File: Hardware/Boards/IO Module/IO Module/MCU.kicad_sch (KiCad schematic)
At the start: 0 parts

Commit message: Updated IO Module Schematics
Added Power, USB hub and USB-JTAG circuits
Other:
- company: (none) -> Drexel University
- title: (none) -> MCU
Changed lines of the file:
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@@
 	(generator "eeschema")
 	(generator_version "8.0")
-	(paper "A4")
+	(paper "A3")
+	(title_block
+		(title "MCU")
+		(date "2024-07-14")
+		(rev "1.0")
+		(company "Drexel University")
+		(comment 1 "Designed by John Hofmeyr")
+	)
 )

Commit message: Updated IO Module Schematics
Added MCU, JTAG and FIFO circuits
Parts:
- added C100, C101: 18pF, Capacitor_SMD:C_0402_1005Metric, symbol Device:C_Small
- added C102, C103, C104, C105, C106, C107, C108, C109, C110, C112: 100nF, Capacitor_SMD:C_0402_1005Metric, symbol Device:C_Small
- added D6: MCU Heartbeat, LED_SMD:LED_0603_1608Metric, symbol Device:LED
- added R66: 10K, Resistor_SMD:R_0402_1005Metric, symbol Device:R_US
- added R67: 1K, Resistor_SMD:R_0402_1005Metric, symbol Device:R_US
- added SW2: RST, Button_Switch_SMD:SW_SPST_PTS645, symbol Switch:SW_SPST
- added TP3, TP4: TestPoint, TestPoint:TestPoint_Pad_D1.0mm, symbol Connector:TestPoint
- added U17: RP2040, Package_DFN_QFN:QFN-56-1EP_7x7mm_P0.4mm_EP3.2x3.2mm, symbol MCU_RaspberryPi:RP2040
- added U19: W25Q16JVUXIQ TR, FursuitTurbofan:USON-8_UX_2x3x0p6_WIN, symbol Memory_Flash:W25Q16JVUXIQ_TR
- added Y5: 12Mhz, Oscillator:Oscillator_SMD_Abracon_ASE-4Pin_3.2x2.5mm, symbol Device:Crystal_GND24_Small
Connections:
- new net: TP3.1, U17.24 (SWCLK)
- new net: TP4.1, U17.25 (SWD)
- new net: R67.1, U17.37 (GPIO25)
- new net: R66.2, SW2.2 (B)
- new net: D6.2 (A), R67.2
- new net +3V3: C105.1, C106.1, C107.1, C108.1, C109.1, C110.1, C112.1, U17.1 (IOVDD), U17.10 (IOVDD), U17.22 (IOVDD), U17.33 (IOVDD), U17.42 (IOVDD), U17.43 (ADC_AVDD), U17.44 (VREG_IN), U17.48 (USB_VDD), U17.49 (IOVDD), U19.8 (VCC)
- new net GND: C100.2, C101.2, C102.2, C103.2, C104.2, C105.2, C106.2, C107.2, C108.2, C109.2, C110.2, C112.2, D6.1 (K), SW2.1 (A), U17.19 (TESTEN), U17.57 (GND), U19.4 (GND), U19.9 (EPAD), Y5.2, Y5.4
- new net I2C0_SCL: U17.7 (GPIO5)
- new net I2C0_SDA: U17.6 (GPIO4)
- new net I2C1_SCL: U17.9 (GPIO7)
- new net I2C1_SDA: U17.8 (GPIO6)
- new net MBUS_D0: U17.11 (GPIO8)
- new net MBUS_D1: U17.12 (GPIO9)
- new net MBUS_D10: U17.29 (GPIO18)
- new net MBUS_D11: U17.30 (GPIO19)
- new net MBUS_D12: U17.31 (GPIO20)
- new net MBUS_D13: U17.32 (GPIO21)
- new net MBUS_D14: U17.34 (GPIO22)
- new net MBUS_D15: U17.35 (GPIO23)
- new net MBUS_D2: U17.13 (GPIO10)
- new net MBUS_D3: U17.14 (GPIO11)
- new net MBUS_D4: U17.15 (GPIO12)
- new net MBUS_D5: U17.16 (GPIO13)
- new net MBUS_D6: U17.17 (GPIO14)
- new net MBUS_D7: U17.18 (GPIO15)
- new net MBUS_D8: U17.27 (GPIO16)
- new net MBUS_D9: U17.28 (GPIO17)
- new net MCU_1V1: C102.1, C103.1, C104.1, U17.23 (DVDD), U17.45 (VREG_VOUT), U17.50 (DVDD)
- new net MCU_XI: C100.1, U17.20 (XIN), Y5.1
- new net MCU_XO: C101.1, U17.21 (XOUT), Y5.3
- new net QSPI_CLK: U17.52 (QSPI_SCLK), U19.6 (CLK)
- new net QSPI_CS: R66.1, U17.56 (QSPI_SS), U19.1 (/CS)
- new net QSPI_D0: U17.53 (QSPI_SD0), U19.5 (DI(IO0))
- new net QSPI_D1: U17.55 (QSPI_SD1), U19.2 (DO(IO1))
- new net QSPI_D2: U17.54 (QSPI_SD2), U19.3 (/WP(IO2))
- new net QSPI_D3: U17.51 (QSPI_SD3), U19.7 (/HLD/RST(IO3))
- new net USB_MCU_D_N: U17.46 (USB_DM)
- new net USB_MCU_D_P: U17.47 (USB_DP)
- no-connect marks 0 -> 1

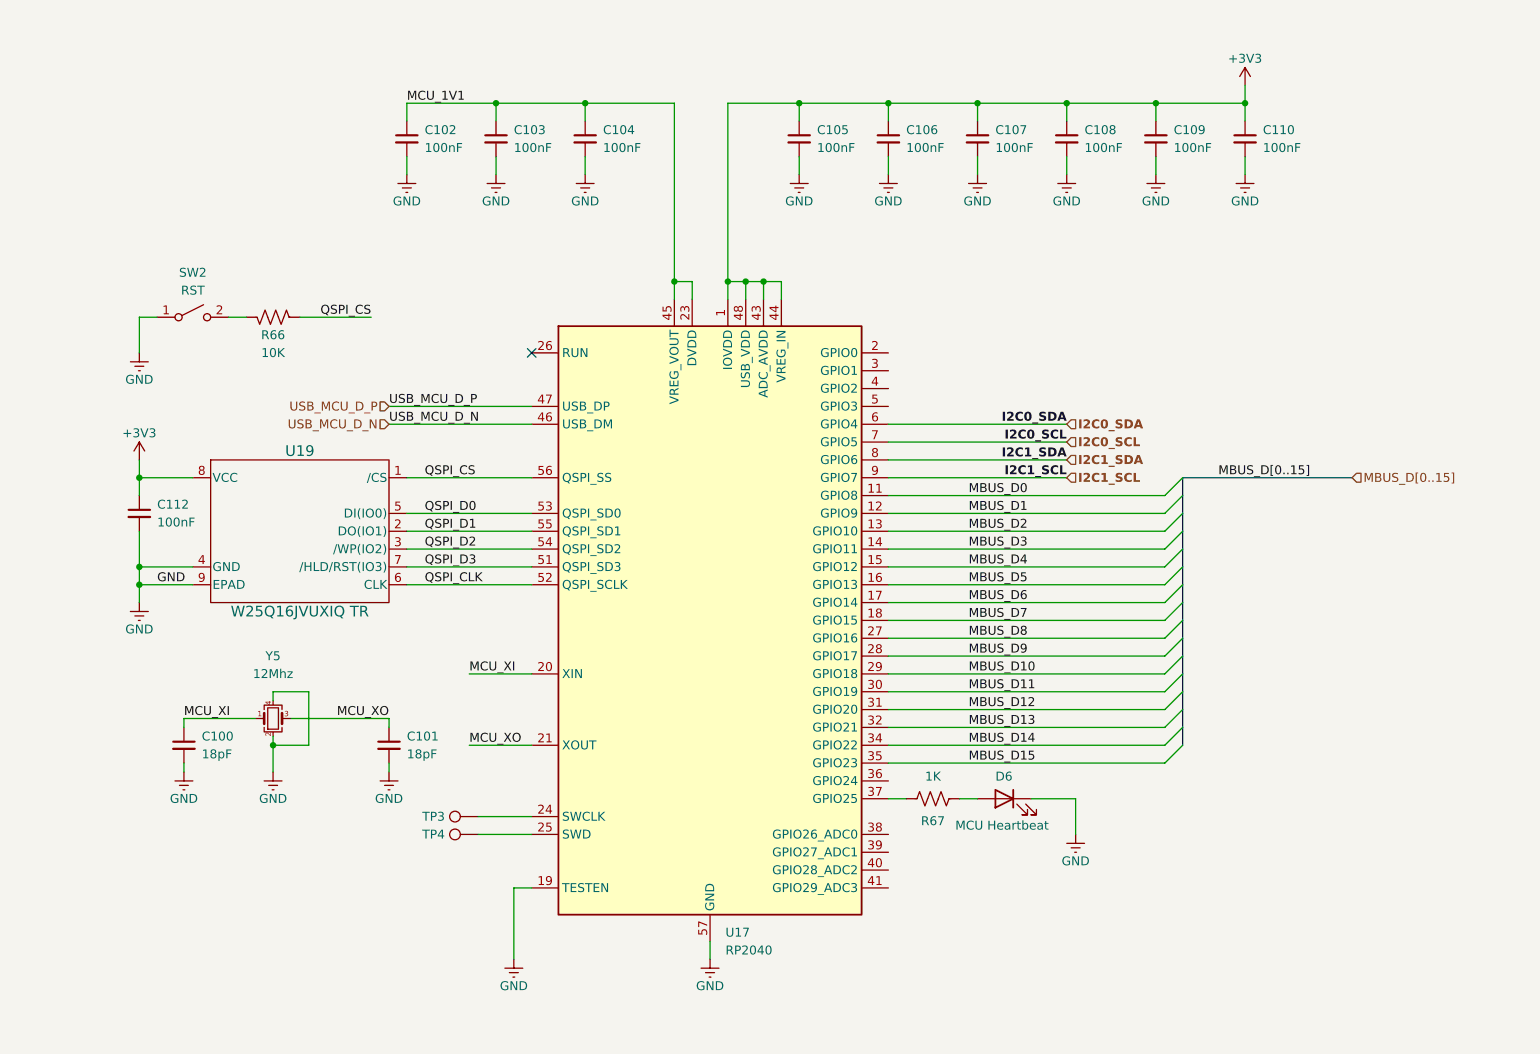
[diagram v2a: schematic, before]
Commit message: Completed IO Module Schematics
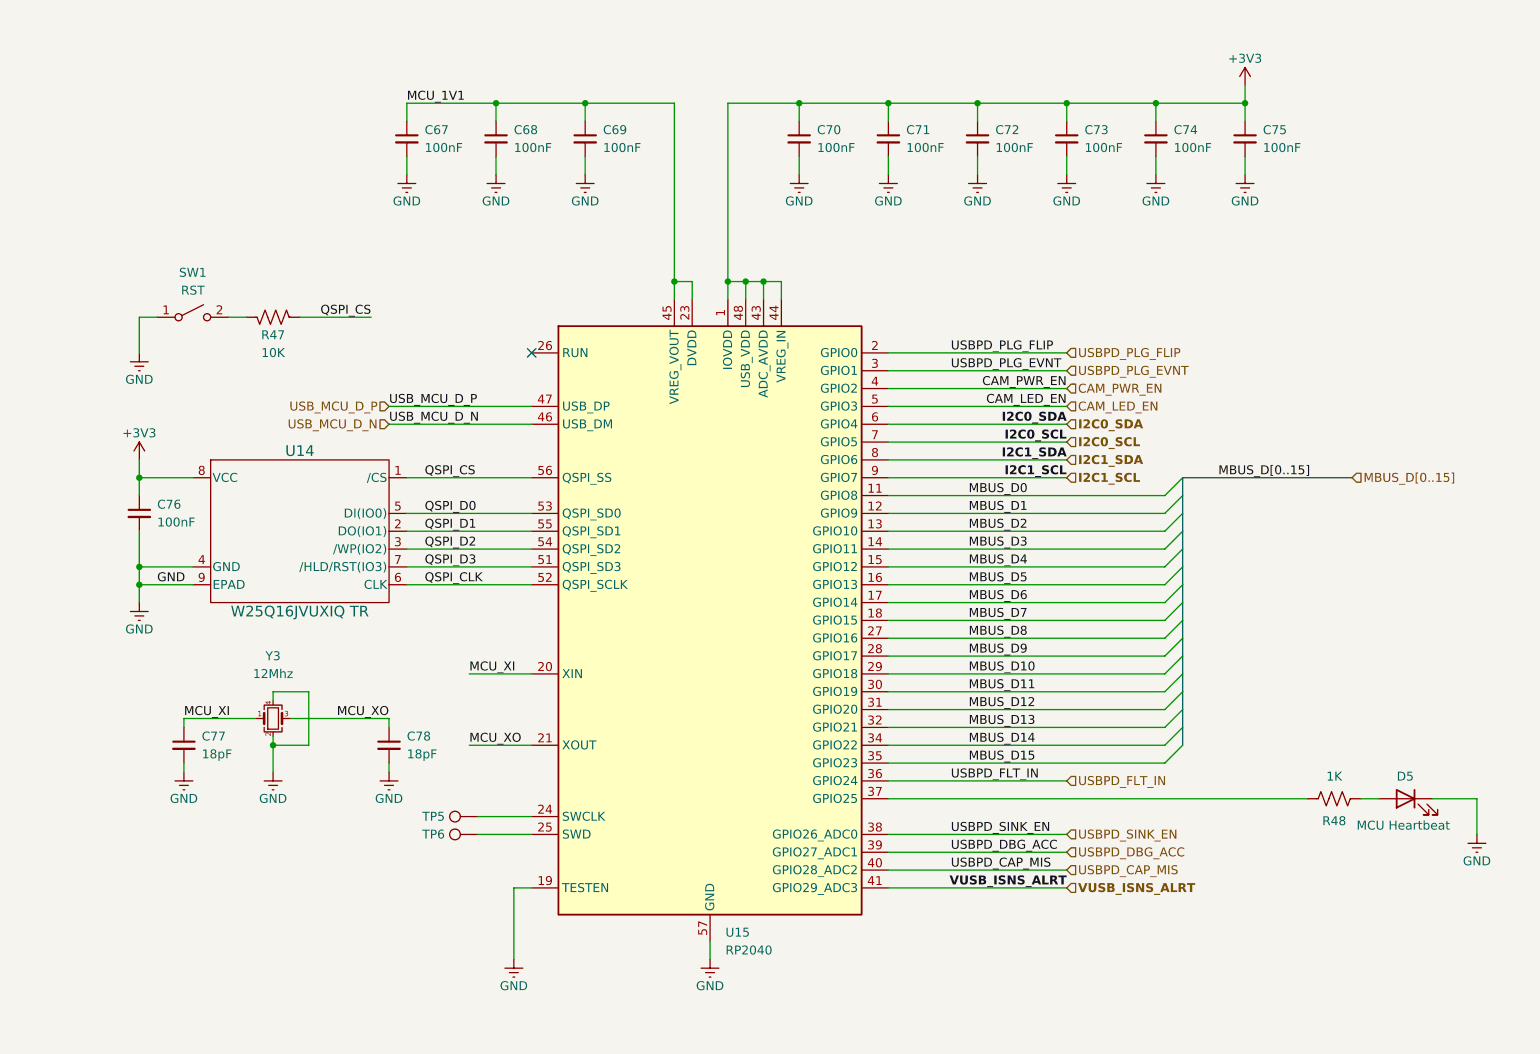
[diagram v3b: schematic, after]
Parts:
- U14: renamed from U19; footprint FursuitTurbofan:USON-8_UX_2x3x0p6_WIN -> IO_Module:USON-8_UX_2x3x0p6_WIN
- renumbered C102 to C67, C103 to C68, C104 to C69, C105 to C70, C106 to C71, C107 to C72, C108 to C73, C109 to C74, C110 to C75, C112 to C76, C100 to C77, C101 to C78, D6 to D5, R66 to R47, R67 to R48, SW2 to SW1, TP3 to TP5, TP4 to TP6, U17 to U15, Y5 to Y3
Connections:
- net USBPD_PLG_FLIP: now reaches U15.2 (GPIO0)
- net USBPD_PLG_EVNT: now reaches U15.3 (GPIO1)
- net USBPD_FLT_IN: now reaches U15.36 (GPIO24)
- net USBPD_SINK_EN: now reaches U15.38 (GPIO26_ADC0)
- net USBPD_DBG_ACC: now reaches U15.39 (GPIO27_ADC1)
- net CAM_PWR_EN: now reaches U15.4 (GPIO2)
- net USBPD_CAP_MIS: now reaches U15.40 (GPIO28_ADC2)
- net VUSB_ISNS_ALRT: now reaches U15.41 (GPIO29_ADC3)
- net CAM_LED_EN: now reaches U15.5 (GPIO3)
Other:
- moved on the sheet: D5, R48

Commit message: Updated SCH with notes & annotations
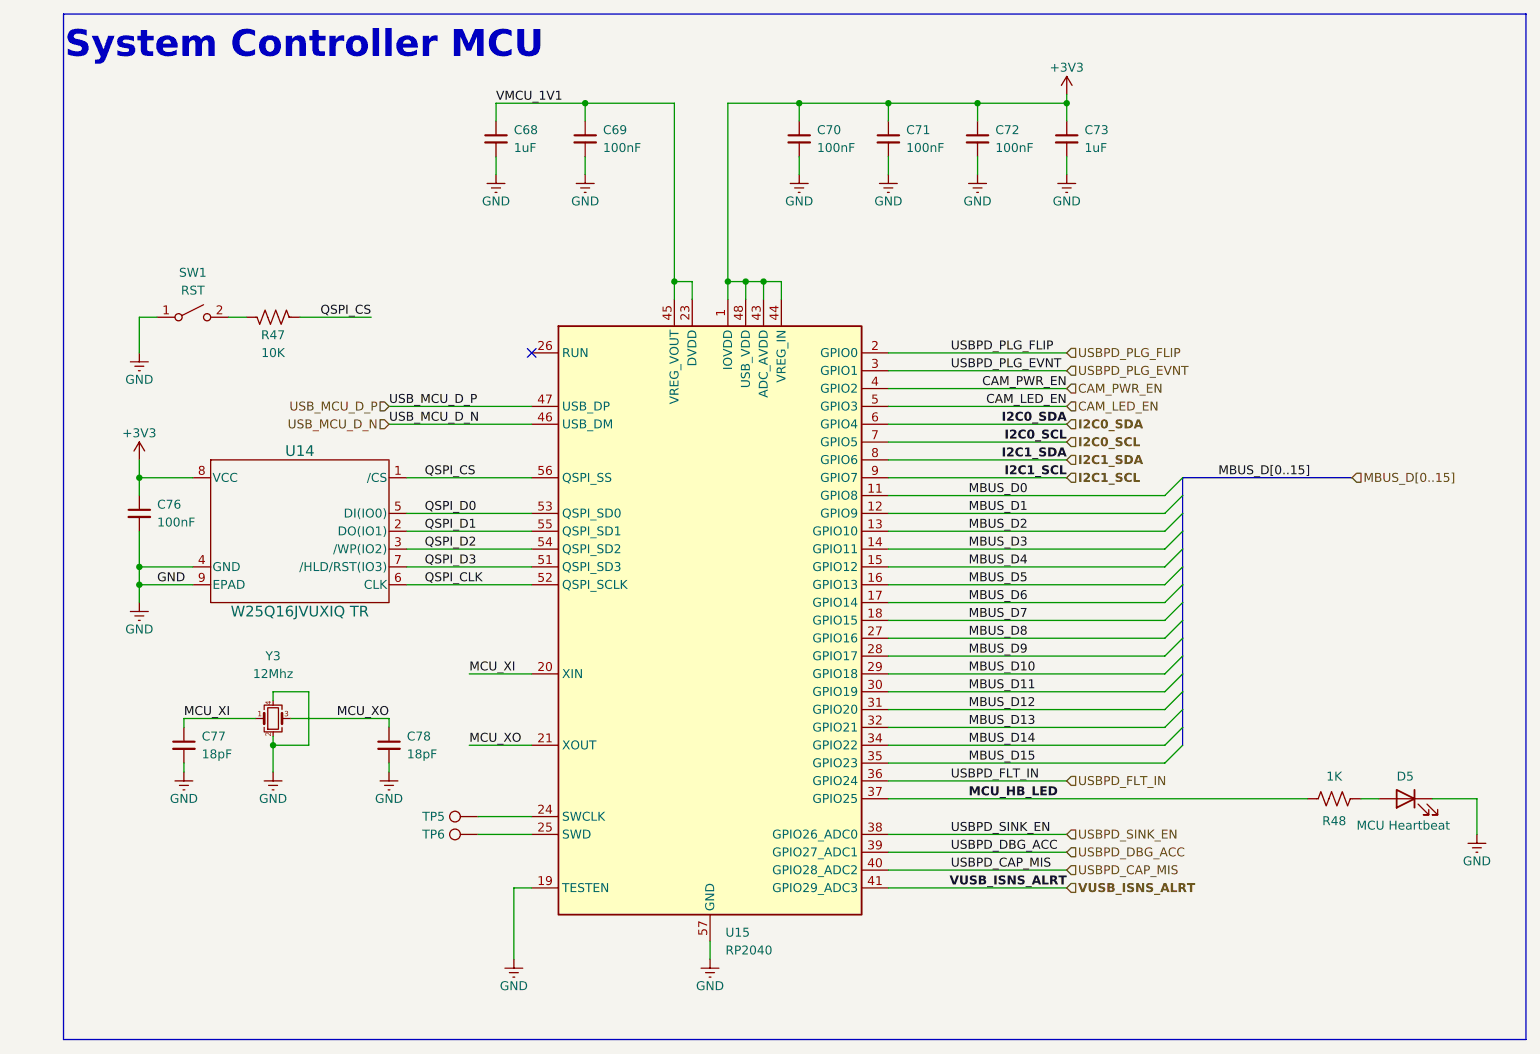
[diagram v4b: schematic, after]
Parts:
- removed C67, C74, C75: 100nF, Capacitor_SMD:C_0402_1005Metric, symbol Device:C_Small
- C68, C73: value 100nF -> 1uF
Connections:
- net MCU_HB_LED: now reaches R48.1, U15.37 (GPIO25)
- net MCU_1V1 renamed VMCU_1V1
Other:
- note added: "System Controller MCU"

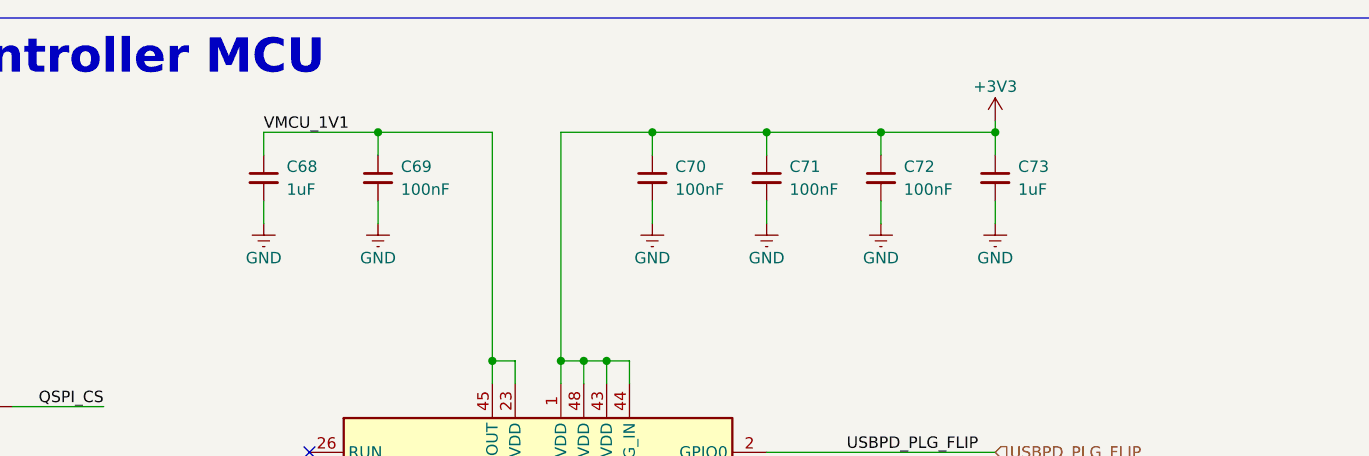
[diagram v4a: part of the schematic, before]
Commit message: Updated PCB routing for IO Module
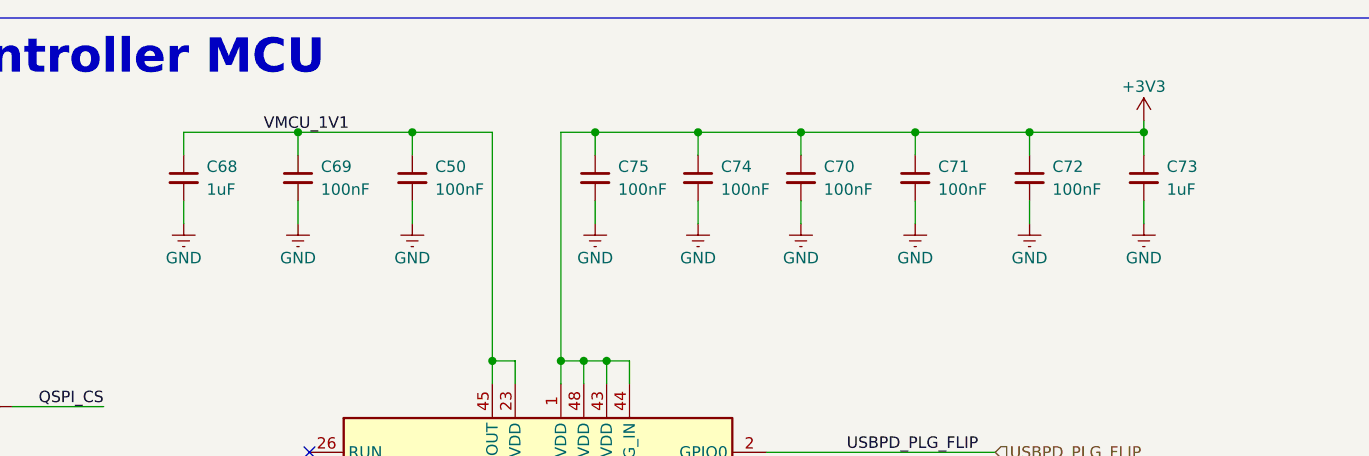
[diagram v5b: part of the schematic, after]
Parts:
- added C50, C74, C75: 100nF, Capacitor_SMD:C_0201_0603Metric, symbol Device:C_Small
- C68, C69, C70, C71, C72, C73, C76, C77, C78: footprint Capacitor_SMD:C_0402_1005Metric -> Capacitor_SMD:C_0201_0603Metric
- R47, R48: footprint Resistor_SMD:R_0402_1005Metric -> Resistor_SMD:R_0201_0603Metric
- SW1: footprint Button_Switch_SMD:SW_SPST_PTS645 -> Button_Switch_SMD:SW_Push_SPST_NO_Alps_SKRK
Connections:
- net +3V3: now also C74.1, C75.1
- net GND: now also C50.2, C74.2, C75.2
- net VMCU_1V1: now also C50.1
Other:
- moved on the sheet: C68, C69, C70, C71, C72, C73
